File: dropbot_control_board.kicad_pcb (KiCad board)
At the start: 4 copper layers, 115 x 92 mm, 139 parts, among them IC1 MCP6024, J1 TFM-105-02-X-DH, P1 CONN_01X01, P10 CONN_01X01, P2 CONN_01X01, P3 CONN_01X04, P4 CONN_01X04, P5 CONN_01X01, P6 USB_B, P7 CONN_01X04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

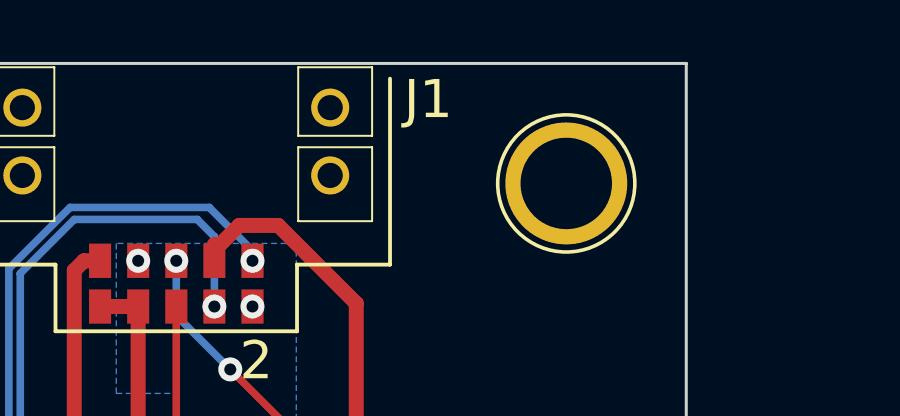
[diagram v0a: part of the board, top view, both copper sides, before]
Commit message: [WIP] Fixes #2: Change prefixes for J1 and IC1
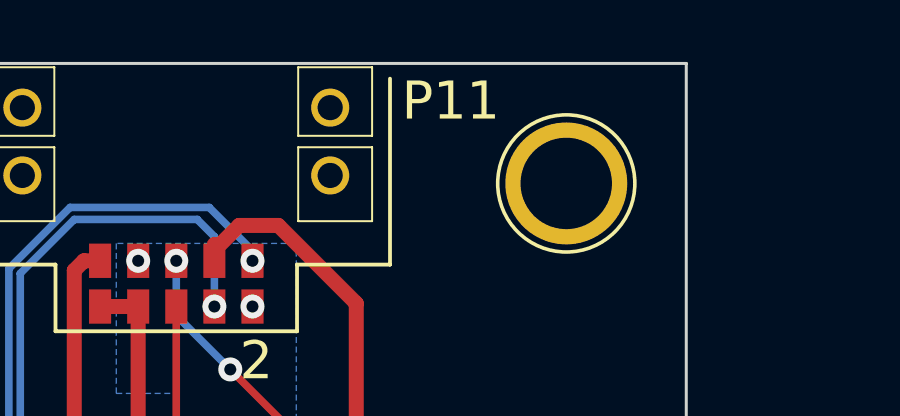
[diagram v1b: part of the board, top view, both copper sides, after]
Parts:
- renumbered J1 to P11, IC1 to U11
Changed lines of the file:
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@@
     (descr "14-lead dip package, row spacing 7.62 mm (300 mils)")
     (tags "dil dip 2.54 300")
-    (fp_text reference IC1 (at 3.575 3.275 180) (layer B.SilkS)
+    (fp_text reference U11 (at 3.575 3.275 180) (layer B.SilkS)
       (effects (font (size 1 1) (thickness 0.15)) (justify mirror))
     )
@@
     (tags "0.050\" DOUBLE HORIZONTAL TERMINAL STRIP.")
     (attr smd)
-    (fp_text reference J1 (at 8.4 1.2) (layer F.SilkS)
+    (fp_text reference P11 (at 9.15 1.25) (layer F.SilkS)
       (effects (font (size 1.27 1.27) (thickness 0.1016)))
     )

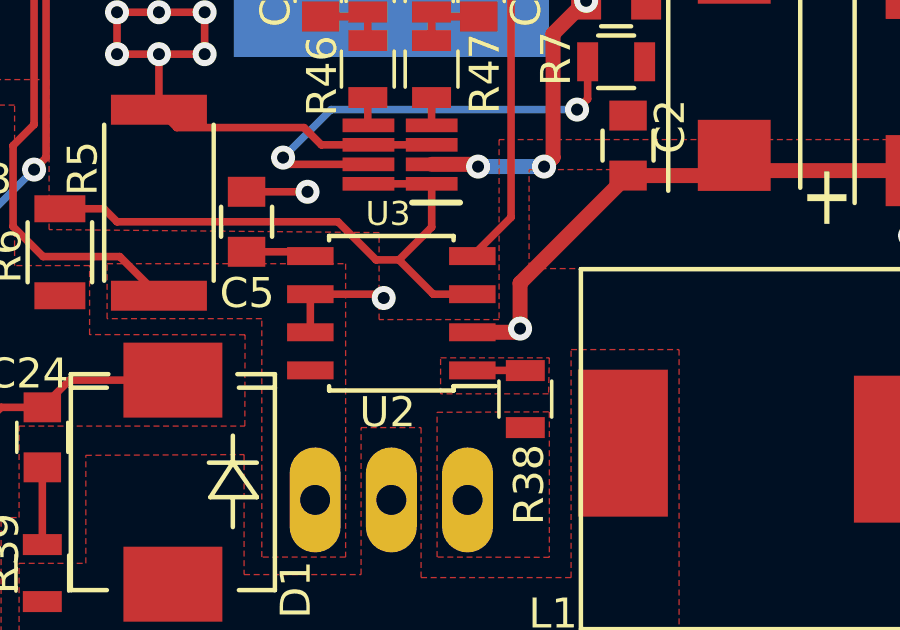
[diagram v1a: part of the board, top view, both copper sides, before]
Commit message: [WIP] Silkscreen fixes (Fixes #4)
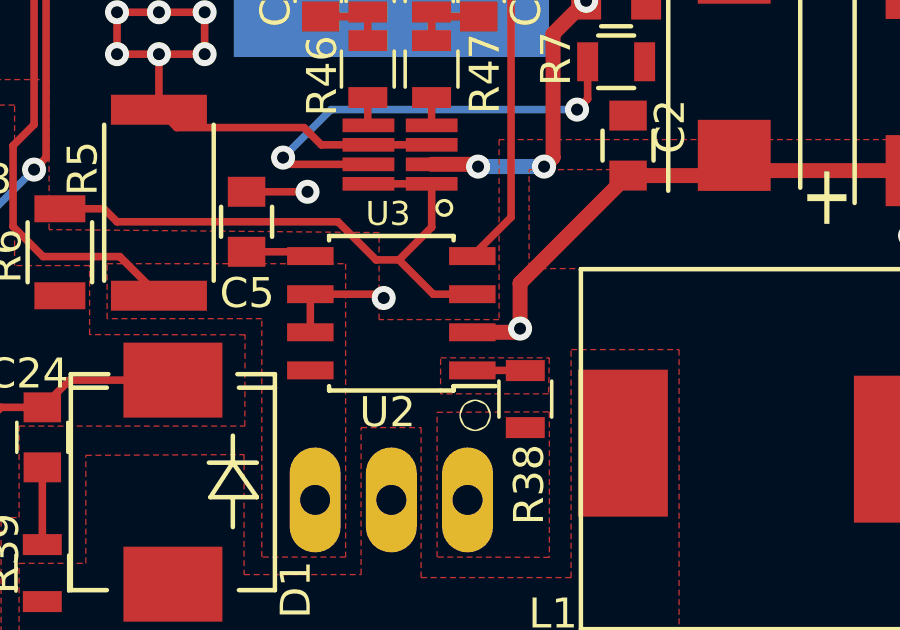
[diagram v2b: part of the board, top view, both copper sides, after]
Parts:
- D5: footprint WheelerLab:wurth-WE-TVS_SOT23-6L -> wurth-WE-TVS_SOT23-6L
- L2: footprint WheelerLab:wurth-WE-CNSW_0805 -> wurth-WE-CNSW_0805
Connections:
- SW1 pad 3: CHASIS_GND -> (no net)
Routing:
- net (no net): track 83.8 -> 84.5 mm, vias 12 -> 13
- net CHASIS_GND: track 12.4 -> 11.7 mm, vias 10 -> 9

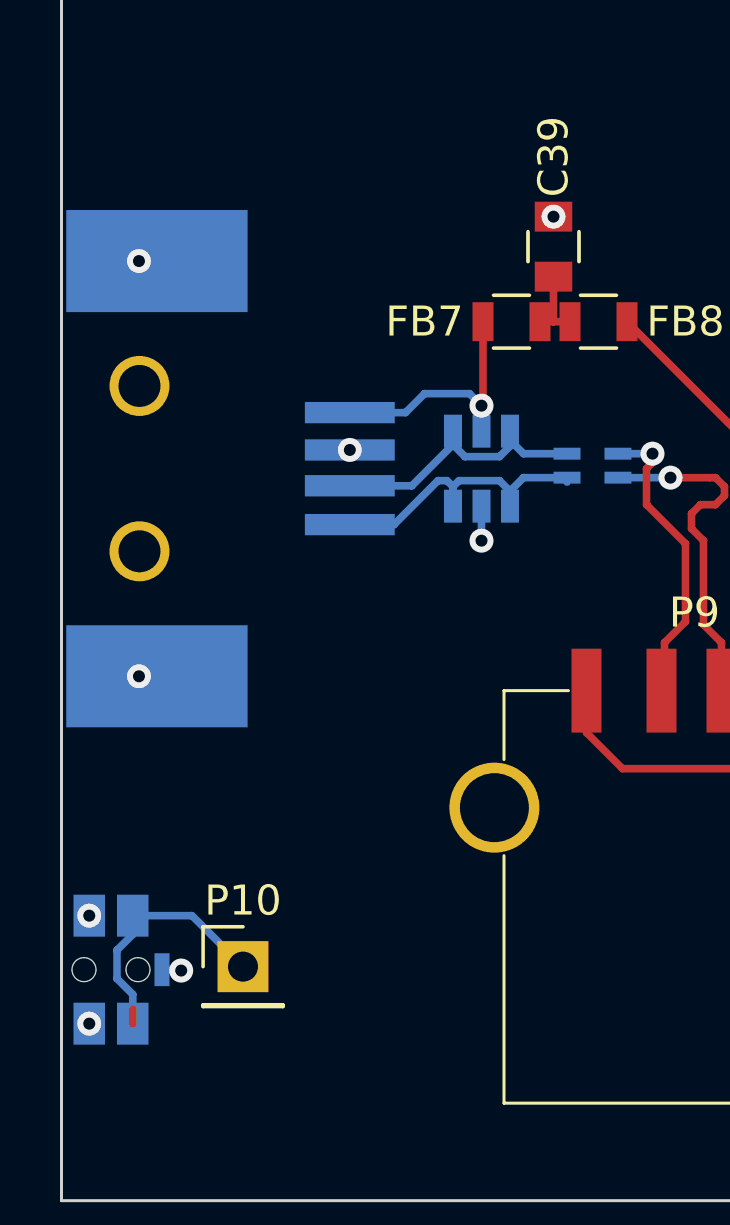
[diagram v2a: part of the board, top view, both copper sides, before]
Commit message: Move USB-B and program switch up 1mm
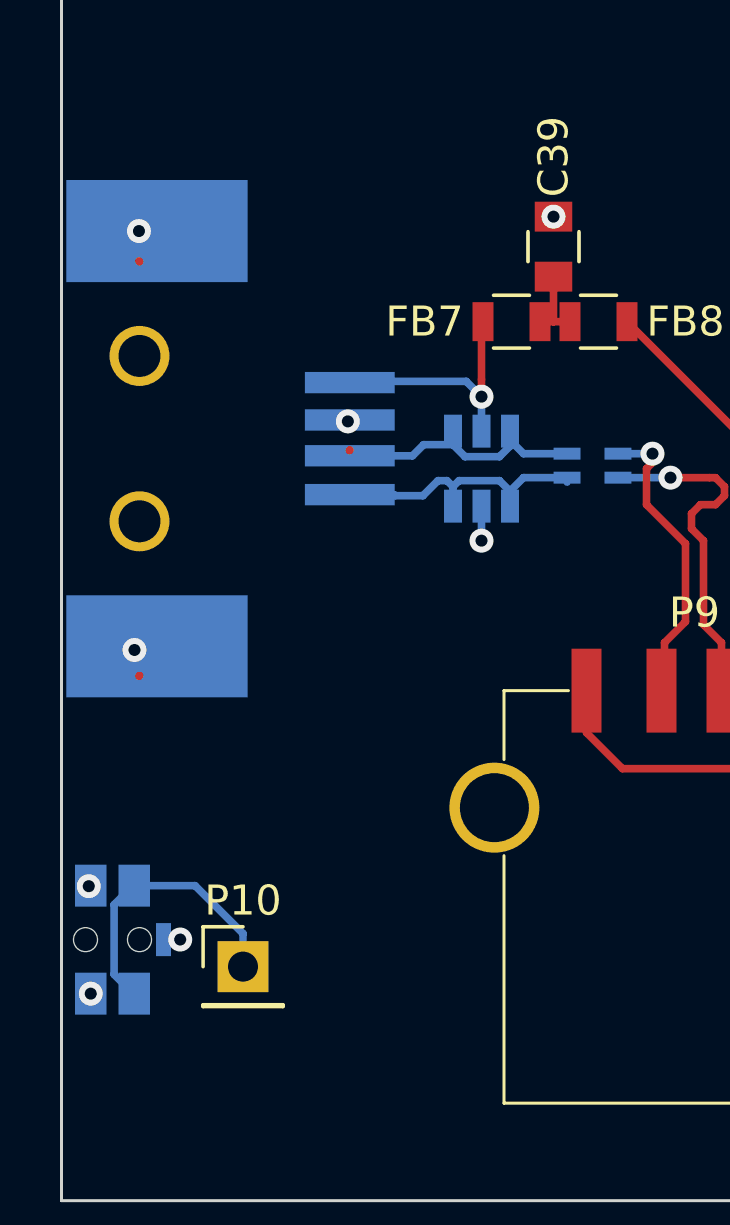
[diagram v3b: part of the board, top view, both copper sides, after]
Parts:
- moved SW1 1.00 mm to (34.7, 82.3)
- moved P6 1.00 mm to (35.6, 65.6)
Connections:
- SW1 pad 3: (no net) -> CHASIS_GND
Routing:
- net CHASIS_GND: track 11.7 -> 3.58 mm, vias 9 -> 10
- net Net-(P10-Pad1): track 8.41 -> 9.68 mm
- net (no net): track 84.5 -> 83.4 mm, vias 13 -> 12

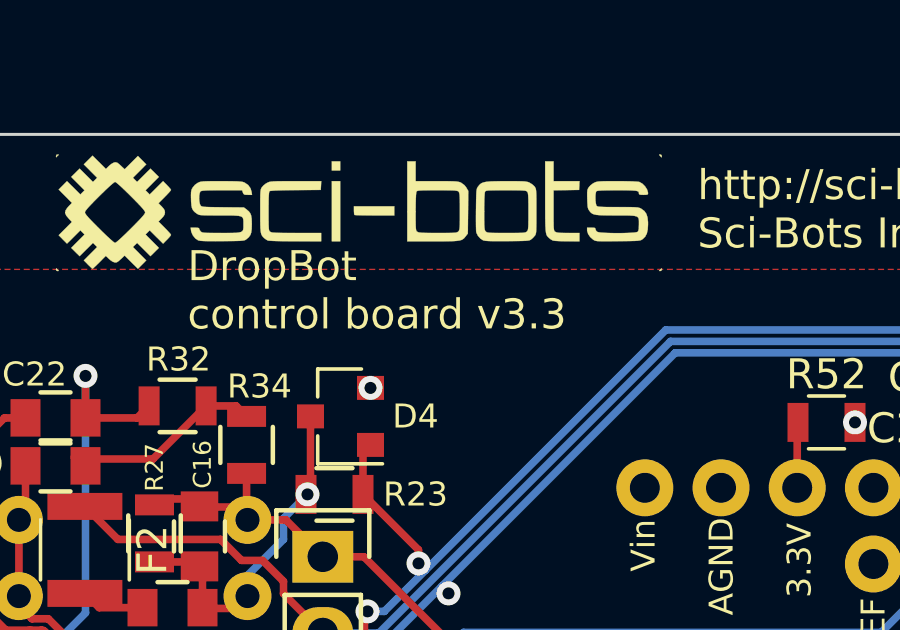
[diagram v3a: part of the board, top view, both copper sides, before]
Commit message: Update outputs and metadata for v3.4
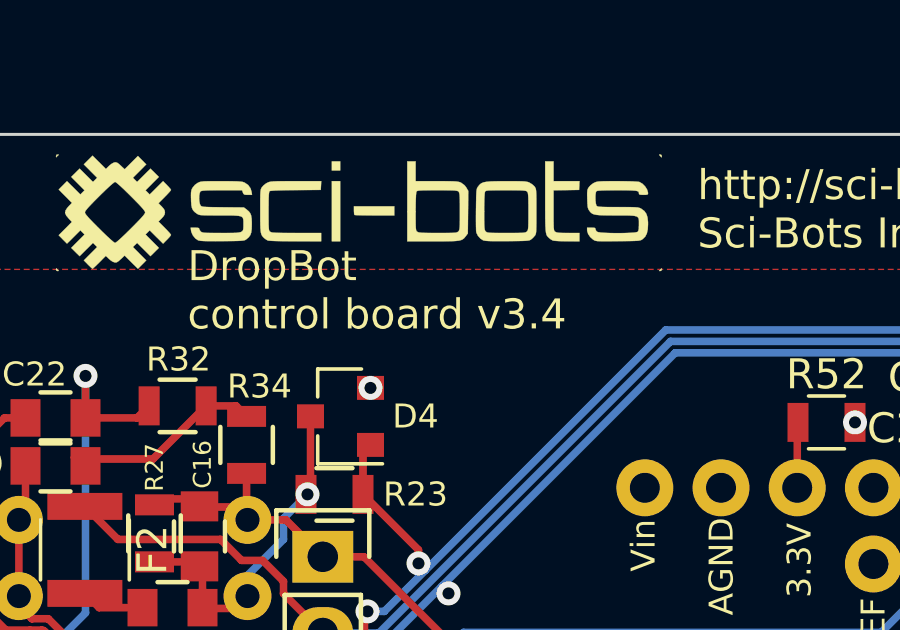
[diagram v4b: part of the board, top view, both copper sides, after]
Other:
- board text added: "DropBot control board v3.4"
- board text removed: "DropBot control board v3.3"
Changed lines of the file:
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@@
-(kicad_pcb (version 4) (host pcbnew 4.0.5)
+(kicad_pcb (version 4) (host pcbnew 4.0.1-stable)
   (general
     (links 299)
     (no_connects 0)
-    (area 24.4875 20.326899 161.254002 113.050001)
+    (area 24.4113 20.326899 161.254002 113.050001)
     (thickness 1.6002)
     (drawings 14)
@@
   (title_block
     (title "DropBot control board")
-    (date 2017-04-04)
-    (rev 3.3)
+    (date 2017-04-25)
+    (rev v3.4)
     (company "Sci-Bots Inc.")
   )
@@
     (effects (font (size 1 1) (thickness 0.2)) (justify left))
   )
-  (gr_text "DropBot\ncontrol board v3.3" (at 75.7 48.2) (layer F.SilkS)
+  (gr_text "DropBot\ncontrol board v3.4" (at 75.7 48.2) (layer F.SilkS)
     (effects (font (size 1 1) (thickness 0.2)) (justify left))
   )
@@
   (segment (start 35.6 59.7) (end 35.6 59.69811) (width 0.254) (layer Front) (net 0))
   (segment (start 35.6 59.69811) (end 35.58166 59.67977) (width 0.254) (layer Front) (net 0))
+  (segment (start 35.6 73.50189) (end 35.58166 73.52023) (width 0.254) (layer Front) (net 0))
+  (segment (start 35.6 73.5) (end 35.6 73.50189) (width 0.254) (layer Front) (net 0))
   (via (at 57.5 74) (size 0.8) (drill 0.4) (layers Front Back) (net 1))
   (segment (start 133 43.45) (end 133 44.6) (width 0.254) (layer Front) (net 1))
@@
   (segment (start 33.95 80.5) (end 33.927 80.5) (width 0.254) (layer Back) (net 93))
   (via (at 33.909 80.518) (size 0.8) (drill 0.4) (layers Front Back) (net 93))
-  (segment (start 35.6 73.50189) (end 35.58166 73.52023) (width 0.254) (layer Front) (net 93))
-  (segment (start 35.6 73.5) (end 35.6 73.50189) (width 0.254) (layer Front) (net 93))
   (segment (start 47 67.84968) (end 47 69) (width 0.254) (layer Back) (net 93))
   (via (at 47 69) (size 0.8) (drill 0.4) (layers Front Back) (net 93))

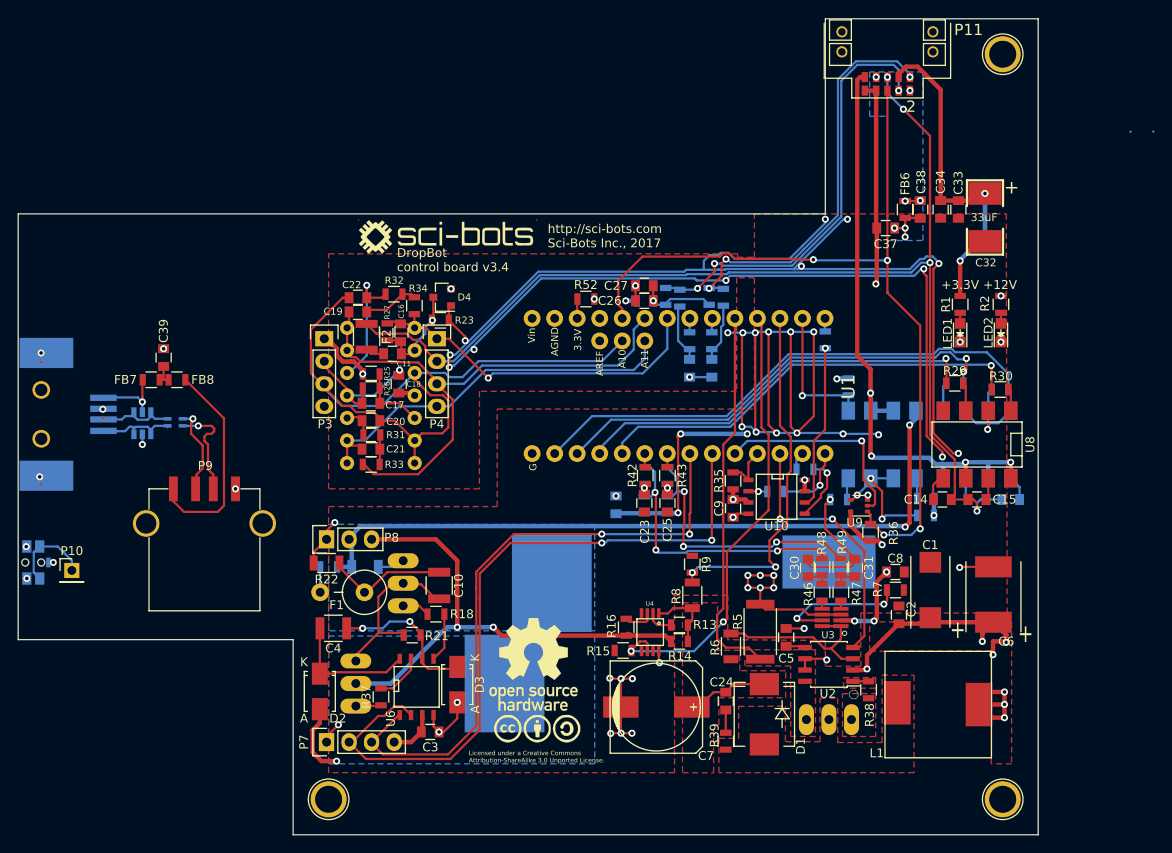
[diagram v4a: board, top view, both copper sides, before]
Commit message: Fix feedback and on-board calibration and move USB
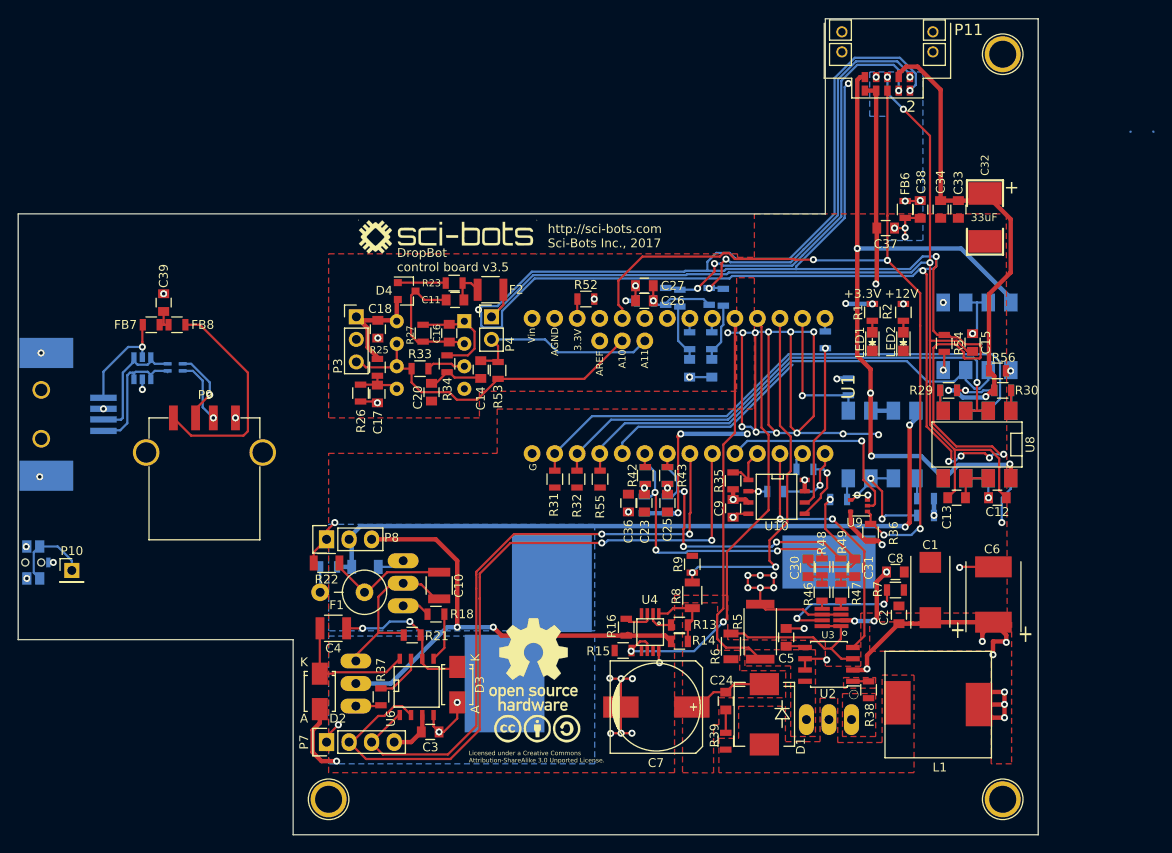
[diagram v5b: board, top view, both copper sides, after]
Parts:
- removed C19: 0.015uF, Capacitors_SMD:C_0805
- removed C21: 470pF, Capacitors_SMD:C_0805
- removed C22: 100pF, Capacitors_SMD:C_0805
- added R53: 1Meg, Resistors_SMD:R_0805, F.Cu at (87.1, 60.6)
- added R54: 200, Resistors_SMD:R_0805, F.Cu at (137.4, 57.6)
- added R55: 5.1k, Resistors_SMD:R_0805, F.Cu at (98.6, 72.9)
- added R56: 200, Resistors_SMD:R_0805, F.Cu at (143.4, 60.7)
- added U12: DPST (2 Form A), 350V, SMD_Packages:DIP-8_SMD, B.Cu at (141.1, 56.8)
- C12, C13, C36: moved to F.Cu
- C14: value 100pF -> 1uF
- C15: value 1nF -> 100pF
- C16: value 0.1uF -> 0.15uF
- P3: value CONN_01X04 -> CONN_01X03; footprint Pin_Headers:Pin_Header_Straight_1x04 -> Pin_Headers:Pin_Header_Straight_1x03_Pitch2.54mm
- P4: value CONN_01X04 -> CONN_01X02; footprint Pin_Headers:Pin_Header_Straight_1x04 -> Pin_Headers:Pin_Header_Straight_1x02_Pitch2.54mm
- R10, R35, R36: value 4.75k -> 5.1k
- R27: value 1Meg -> 100k
- R31: value 18.7k -> 5.1k
- R32: value 2.1k -> 5.1k
- R33: value 14.7k -> 100k
- R34: value 887 -> 5.1k
- U11: value MCP6024 -> MCP6022; footprint Housings_DIP:DIP-14_W7.62mm -> Housings_DIP:DIP-8_W7.62mm
- moved C14 54.1 mm to (85.2, 60.5), turned to 90 degrees
- moved R32 29.3 mm to (96.0, 72.9), turned to 270 degrees
- moved R31 21.2 mm to (93.5, 72.9), turned to 270 degrees
- moved C15 17.7 mm to (140.6, 57.5), turned to 270 degrees
- moved F2 14.9 mm to (86.2, 51.5), turned to 0 degrees
- moved R33 12.1 mm to (78.3, 60.5)
- moved LED2 11.0 mm to (132.8, 57.4)
- moved R2 11.0 mm to (132.8, 54.1)
- moved LED1 9.95 mm to (129.3, 57.4)
- moved R1 9.94 mm to (129.3, 54.1)
- moved C11 9.31 mm to (82.2, 52.7)
- moved P9 8.00 mm to (54.0, 66.0)
- moved C20 7.55 mm to (79.6, 63.1), turned to 90 degrees
- moved R34 7.51 mm to (81.3, 59.9)
- moved C18 6.63 mm to (73.5, 56.0), turned to 270 degrees
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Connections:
- C14 pad 2: CUR_SENSE -> A11
- C16 pad 1: A6 -> Net-(C16-Pad1)
- C16 pad 2: Net-(C11-Pad1) -> Net-(C11-Pad2)
- C20 pad 1: +0.6V -> GND
- C20 pad 2: Net-(C20-Pad2) -> Net-(C14-Pad1)
- D4 pad 3: Net-(C11-Pad1) -> Net-(C11-Pad2)
- F2 pad 1: CUR_SENSE -> Net-(C11-Pad1)
- F2 pad 2: Net-(C11-Pad2) -> CUR_SENSE
- P4 pad 1: A6 -> CUR_SENSE
- P4 pad 2: CUR_SENSE -> A11
- R24 pad 1: D0 -> GND
- R27 pad 1: A6 -> Net-(C16-Pad1)
- R27 pad 2: Net-(C11-Pad1) -> Net-(C11-Pad2)
- R28 pad 1: D1 -> +3.3V
- R29 pad 1: D2 -> GND
- R30 pad 1: D3 -> +3.3V
- R31 pad 1: Net-(C21-Pad2) -> D0
- R31 pad 2: Net-(C20-Pad2) -> GND
- R32 pad 1: Net-(C19-Pad2) -> D1
- R32 pad 2: Net-(C22-Pad2) -> GND
- R33 pad 1: A7 -> +0.6V
- R33 pad 2: Net-(C21-Pad2) -> Net-(R33-Pad2)
- R34 pad 1: A6 -> Net-(C14-Pad1)
- R34 pad 2: Net-(C19-Pad2) -> Net-(C16-Pad1)
- U11 pad 1: A6 -> Net-(C16-Pad1)
- U11 pad 2: Net-(C11-Pad1) -> Net-(C11-Pad2)
- U11 pad 3: +0.6V -> Net-(R33-Pad2)
- U11 pad 4: +3.3V -> GND
- U11 pad 8: A11 -> +3.3V
- U7 pad 2: GND -> D0
- U7 pad 3: Net-(R24-Pad2) -> D0
- U7 pad 4: GND -> Net-(R24-Pad2)
- U7 pad 5: Net-(C12-Pad1) -> GND
- U7 pad 6: VOUT -> Net-(C12-Pad1)
- U7 pad 7: Net-(C13-Pad1) -> Net-(C12-Pad1)
- U8 pad 2: GND -> D1
- U8 pad 3: Net-(R29-Pad2) -> D1
- U8 pad 4: GND -> Net-(R29-Pad2)
- U8 pad 5: Net-(C14-Pad1) -> GND
- U8 pad 6: VOUT -> Net-(C13-Pad1)
- U8 pad 7: Net-(C15-Pad1) -> Net-(C13-Pad1)
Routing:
- net A7: track 63.7 -> 0.00 mm
- net GND: track 313.9 -> 359.1 mm, vias 48 -> 44
- net +0.6V: track 80.2 -> 38.0 mm
- net A6: track 40.9 -> 0.00 mm, vias 1 -> 0
- net D3: track 49.2 -> 24.1 mm, vias 1 -> 0
- net A11: track 43.9 -> 23.3 mm
- net VOUT: track 73.9 -> 89.0 mm
- net Net-(C22-Pad2): track 14.9 -> 0.00 mm, vias 1 -> 0
- net +3.3V: track 101.7 -> 116.2 mm, vias 17 -> 18
- net Net-(C11-Pad2): track 2.12 -> 15.5 mm
- net Net-(C16-Pad1): track 0.00 -> 11.8 mm
- net D1: track 51.9 -> 60.8 mm, vias 2 -> 1
- net D2: track 46.6 -> 54.9 mm, vias 1 -> 0
- net Net-(C11-Pad1): track 12.1 -> 3.97 mm, vias 1 -> 0
- net D0: track 59.0 -> 66.5 mm
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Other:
- board text added: "DropBot control board v3.5"
- board text removed: "DropBot control board v3.4"
